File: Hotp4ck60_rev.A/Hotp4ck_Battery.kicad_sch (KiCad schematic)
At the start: 16 parts, among them J3 Conn_01x02_MountingPin, Q1 AO3401A, SW2 PWR, U3 MAX17048, U3 TP4056

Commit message: Fixed path
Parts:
- renumbered C21 to C22, C23 to C24
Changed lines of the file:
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@@
   (symbol (lib_id "Device:C_Small") (at 40.64 53.34 0) (unit 1)
     (in_bom yes) (on_board yes) (dnp no)
-    (property "Reference" "C21" (at 40.64 45.72 0)
+    (property "Reference" "C22" (at 40.64 45.72 0)
       (effects (font (size 1.27 1.27)))
     )
@@
       (project "Hotp4ck60"
         (path "/a57939d7-40ce-4436-8014-db245ef7f3c5/18c06ada-111b-4ec0-9dc0-78c3052676b0"
-          (reference "C21") (unit 1)
+          (reference "C22") (unit 1)
         )
       )
@@
   (symbol (lib_id "Device:C_Small") (at 83.82 119.38 0) (unit 1)
     (in_bom yes) (on_board yes) (dnp no) (fields_autoplaced)
-    (property "Reference" "C27" (at 81.28 118.1162 0)
-      (effects (font (size 1.27 1.27)) (justify right))
-    )
-    (property "Value" "100 nF" (at 81.28 120.6562 0)
-      (effects (font (size 1.27 1.27)) (justify right))
+    (property "Reference" "C27" (at 86.36 118.1163 0)
+      (effects (font (size 1.27 1.27)) (justify left))
+    )
+    (property "Value" "100 nF" (at 86.36 120.6563 0)
+      (effects (font (size 1.27 1.27)) (justify left))
     )
     (property "Footprint" "Capacitor_SMD:C_0402_1005Metric" (at 83.82 119.38 0)
@@
         )
         (path "/a57939d7-40ce-4436-8014-db245ef7f3c5/18c06ada-111b-4ec0-9dc0-78c3052676b0"
-          (reference "C27") (unit 1)
+          (reference "C25") (unit 1)
         )
       )
@@
   (symbol (lib_id "Device:C_Small") (at 77.47 53.34 0) (unit 1)
     (in_bom yes) (on_board yes) (dnp no)
-    (property "Reference" "C23" (at 73.66 52.07 0)
+    (property "Reference" "C24" (at 73.66 52.07 0)
       (effects (font (size 1.27 1.27)) (justify right))
     )
@@
       (project "Hotp4ck60"
         (path "/a57939d7-40ce-4436-8014-db245ef7f3c5/18c06ada-111b-4ec0-9dc0-78c3052676b0"
+          (reference "C24") (unit 1)
+        )
+      )
+      (project "designguide-schematic"
+        (path "/c2a65ddb-3915-4293-98a9-444287fe2a3d"
+          (reference "C2") (unit 1)
+        )
+      )
+    )
+  )
+  (symbol (lib_id "Device:R_Small") (at 35.56 58.42 0) (unit 1)
+    (in_bom yes) (on_board yes) (dnp no)
+    (property "Reference" "R6" (at 29.21 57.15 0)
+      (effects (font (size 1.27 1.27)) (justify left))
+    )
+    (property "Value" "1.5 kOhm" (at 25.4 59.69 0)
+      (effects (font (size 1.27 1.27)) (justify left))
+    )
+    (property "Footprint" "Resistor_SMD:R_0402_1005Metric" (at 35.56 58.42 0)
+      (effects (font (size 1.27 1.27)) hide)
+    )
+    (property "Datasheet" "~" (at 35.56 58.42 0)
+      (effects (font (size 1.27 1.27)) hide)
+    )
+    (property "LCSC" "C25792" (at 35.56 58.42 0)
+      (effects (font (size 1.27 1.27)) hide)
+    )
+    (pin "1")
+    (pin "2")
+    (instances
+      (project "osprey_rev_a"
+        (path "/86a516b3-939b-48ee-9a25-d0111c577d06/e12a0b82-f794-4b5e-b657-628292a2530a"
+          (reference "R6") (unit 1)
+        )
+      )
+      (project "Hotp4ck60"
+        (path "/a57939d7-40ce-4436-8014-db245ef7f3c5"
+          (reference "R3") (unit 1)
+        )
+        (path "/a57939d7-40ce-4436-8014-db245ef7f3c5/18c06ada-111b-4ec0-9dc0-78c3052676b0"
+          (reference "R3") (unit 1)
+        )
+      )
+      (project "designguide-schematic"
+        (path "/c2a65ddb-3915-4293-98a9-444287fe2a3d"
+          (reference "R5") (unit 1)
+        )
+      )
+    )
+  )
+  (symbol (lib_id "Device:C_Small") (at 46.99 53.34 0) (unit 1)
+    (in_bom yes) (on_board yes) (dnp no)
+    (property "Reference" "C22" (at 46.99 45.72 0)
+      (effects (font (size 1.27 1.27)))
+    )
+    (property "Value" "4.7 uF" (at 46.99 48.26 0)
+      (effects (font (size 1.27 1.27)))
+    )
+    (property "Footprint" "Capacitor_SMD:C_0402_1005Metric" (at 46.99 53.34 0)
+      (effects (font (size 1.27 1.27)) hide)
+    )
+    (property "Datasheet" "~" (at 46.99 53.34 0)
+      (effects (font (size 1.27 1.27)) hide)
+    )
+    (property "LCSC" "C52923" (at 46.99 53.34 0)
+      (effects (font (size 1.27 1.27)) hide)
+    )
+    (property "Notes" "X7R, 10%" (at 46.99 53.34 0)
+      (effects (font (size 1.27 1.27)) hide)
+    )
+    (pin "1")
+    (pin "2")
+    (instances
+      (project "osprey_rev_a"
+        (path "/86a516b3-939b-48ee-9a25-d0111c577d06/e12a0b82-f794-4b5e-b657-628292a2530a"
+          (reference "C22") (unit 1)
+        )
+      )
+      (project "Hotp4ck60"
+        (path "/a57939d7-40ce-4436-8014-db245ef7f3c5"
+          (reference "C22") (unit 1)
+        )
+        (path "/a57939d7-40ce-4436-8014-db245ef7f3c5/18c06ada-111b-4ec0-9dc0-78c3052676b0"
           (reference "C23") (unit 1)
         )
       )
-      (project "designguide-schematic"
-        (path "/c2a65ddb-3915-4293-98a9-444287fe2a3d"
-          (reference "C2") (unit 1)
-        )
-      )
-    )
-  )
-  (symbol (lib_id "Device:R_Small") (at 35.56 58.42 0) (unit 1)
-    (in_bom yes) (on_board yes) (dnp no)
-    (property "Reference" "R6" (at 29.21 57.15 0)
-      (effects (font (size 1.27 1.27)) (justify left))
-    )
-    (property "Value" "1.5 kOhm" (at 25.4 59.69 0)
-      (effects (font (size 1.27 1.27)) (justify left))
-    )
-    (property "Footprint" "Resistor_SMD:R_0402_1005Metric" (at 35.56 58.42 0)
-      (effects (font (size 1.27 1.27)) hide)
-    )
-    (property "Datasheet" "~" (at 35.56 58.42 0)
-      (effects (font (size 1.27 1.27)) hide)
-    )
-    (property "LCSC" "C25792" (at 35.56 58.42 0)
-      (effects (font (size 1.27 1.27)) hide)
-    )
-    (pin "1")
-    (pin "2")
-    (instances
-      (project "osprey_rev_a"
-        (path "/86a516b3-939b-48ee-9a25-d0111c577d06/e12a0b82-f794-4b5e-b657-628292a2530a"
-          (reference "R6") (unit 1)
-        )
-      )
-      (project "Hotp4ck60"
-        (path "/a57939d7-40ce-4436-8014-db245ef7f3c5"
-          (reference "R3") (unit 1)
-        )
-        (path "/a57939d7-40ce-4436-8014-db245ef7f3c5/18c06ada-111b-4ec0-9dc0-78c3052676b0"
-          (reference "R3") (unit 1)
-        )
-      )
-      (project "designguide-schematic"
-        (path "/c2a65ddb-3915-4293-98a9-444287fe2a3d"
-          (reference "R5") (unit 1)
-        )
-      )
-    )
-  )
-  (symbol (lib_id "Device:C_Small") (at 46.99 53.34 0) (unit 1)
-    (in_bom yes) (on_board yes) (dnp no)
-    (property "Reference" "C22" (at 46.99 45.72 0)
-      (effects (font (size 1.27 1.27)))
-    )
-    (property "Value" "4.7 uF" (at 46.99 48.26 0)
-      (effects (font (size 1.27 1.27)))
-    )
-    (property "Footprint" "Capacitor_SMD:C_0402_1005Metric" (at 46.99 53.34 0)
-      (effects (font (size 1.27 1.27)) hide)
-    )
-    (property "Datasheet" "~" (at 46.99 53.34 0)
-      (effects (font (size 1.27 1.27)) hide)
-    )
-    (property "LCSC" "C52923" (at 46.99 53.34 0)
-      (effects (font (size 1.27 1.27)) hide)
-    )
-    (property "Notes" "X7R, 10%" (at 46.99 53.34 0)
-      (effects (font (size 1.27 1.27)) hide)
-    )
-    (pin "1")
-    (pin "2")
-    (instances
-      (project "osprey_rev_a"
-        (path "/86a516b3-939b-48ee-9a25-d0111c577d06/e12a0b82-f794-4b5e-b657-628292a2530a"
-          (reference "C22") (unit 1)
-        )
-      )
-      (project "Hotp4ck60"
-        (path "/a57939d7-40ce-4436-8014-db245ef7f3c5"
-          (reference "C22") (unit 1)
-        )
-        (path "/a57939d7-40ce-4436-8014-db245ef7f3c5/18c06ada-111b-4ec0-9dc0-78c3052676b0"
-          (reference "C22") (unit 1)
-        )
-      )

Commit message: Modified positions
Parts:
- renumbered C22 to C21, C24 to C23
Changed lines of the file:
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@@
   (symbol (lib_id "Device:C_Small") (at 40.64 53.34 0) (unit 1)
     (in_bom yes) (on_board yes) (dnp no)
-    (property "Reference" "C22" (at 40.64 45.72 0)
+    (property "Reference" "C21" (at 40.64 45.72 0)
       (effects (font (size 1.27 1.27)))
     )
@@
       (project "Hotp4ck60"
         (path "/a57939d7-40ce-4436-8014-db245ef7f3c5/18c06ada-111b-4ec0-9dc0-78c3052676b0"
-          (reference "C22") (unit 1)
+          (reference "C21") (unit 1)
         )
       )
@@
         )
         (path "/a57939d7-40ce-4436-8014-db245ef7f3c5/18c06ada-111b-4ec0-9dc0-78c3052676b0"
-          (reference "C25") (unit 1)
+          (reference "C24") (unit 1)
         )
       )
@@
   (symbol (lib_id "Device:C_Small") (at 77.47 53.34 0) (unit 1)
     (in_bom yes) (on_board yes) (dnp no)
-    (property "Reference" "C24" (at 73.66 52.07 0)
+    (property "Reference" "C23" (at 73.66 52.07 0)
       (effects (font (size 1.27 1.27)) (justify right))
     )
@@
       (project "Hotp4ck60"
         (path "/a57939d7-40ce-4436-8014-db245ef7f3c5/18c06ada-111b-4ec0-9dc0-78c3052676b0"
-          (reference "C24") (unit 1)
+          (reference "C23") (unit 1)
         )
       )
@@
         )
         (path "/a57939d7-40ce-4436-8014-db245ef7f3c5/18c06ada-111b-4ec0-9dc0-78c3052676b0"
-          (reference "C23") (unit 1)
-        )
-      )
+          (reference "C22") (unit 1)
+        )
+      )

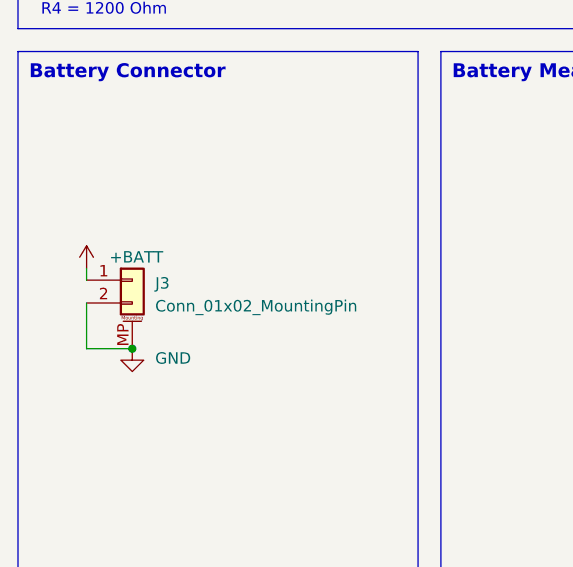
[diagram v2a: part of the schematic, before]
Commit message: unified daughterboard, MCU 추가
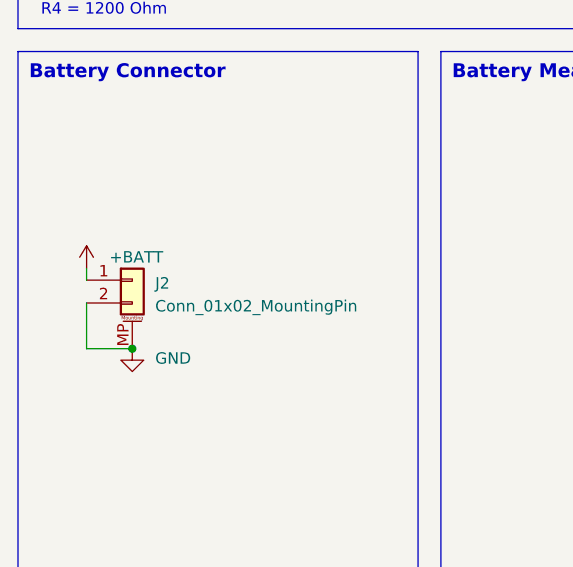
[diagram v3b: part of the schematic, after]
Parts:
- renumbered J3 to J2

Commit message: 리비젼A 수정
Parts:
- removed J2: Conn_01x02_MountingPin, Connector_Molex:Molex_PicoBlade_53261-0271_1x02-1MP_P1.25mm_Horizontal, symbol Connector_Generic_MountingPin:Conn_01x02_MountingPin
- removed SW2: PWR, marbastlib-various:SW_MSK12C02-HB, symbol Connector_Generic_MountingPin:Conn_01x03_MountingPin
- added SW2: SW_DIP_x01, Hotp4ck:SW_DIP_HOTP4CK, symbol Switch:SW_DIP_x01
- renumbered C27 to C24, R6 to R3, R7 to R4, R7 to R6, R1 to R7, R2 to R8, U3 to U4
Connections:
- net +BATT: now also SW2.1
- net at Q1.3 (D): now also SW2.2
- no-connect marks 2 -> 1

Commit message: 배선 완료
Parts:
- removed LED2: Yellow, LED_SMD:LED_0603_1608Metric, symbol Device:LED_Small
- removed U3: TP4056, Package_SO:SOIC-8-1EP_3.9x4.9mm_P1.27mm_EP2.29x3mm, symbol marbastlib-various:TP4056
- added C24, C26: 4u7, Capacitor_SMD:C_0402_1005Metric, symbol Device:C_Small
- added C25, C27: 1u, Capacitor_SMD:C_0402_1005Metric, symbol Device:C_Small
- added R1: 68k, Resistor_SMD:R_0805_2012Metric, symbol Device:R_Small
- added R2: 1k5, Resistor_SMD:R_0402_1005Metric, symbol Device:R_Small
- added U2: BQ24075RGT, Package_DFN_QFN:VQFN-16-1EP_3x3mm_P0.5mm_EP1.6x1.6mm, symbol Battery_Management:BQ24075RGT
- C21, C23: value 10 uF -> 4u7; footprint Capacitor_SMD:C_0805_2012Metric -> Capacitor_SMD:C_0402_1005Metric; LCSC (none) -> C23733
- C22: value 4.7 uF -> 4u7; LCSC C52923 -> C23733; Notes X7R, 10% -> (none)
- R3: value 1.5 kOhm -> 2k2; LCSC C25792 -> C25879
- R4: value 1.2 kOhm -> 10k; LCSC C25867 -> C25744
- U4: now left out of the parts list
- renumbered C24 to C7, R6 to R5, R7 to R6, R8 to R7
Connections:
- net +5V: now also C23.1, U2.13 (IN)
- net +BATT: now also C26.1, C27.1, U2.2 (BAT), U2.3 (BAT); no longer C23.1
- net +VSW: now also C24.1, C25.1, U2.10 (OUT), U2.11 (OUT), U2.6 (EN1)
- net GND: now also R3.2, C24.2, C25.2, C26.2, C27.2, R1.2, R2.2, U2.15 (SYSOFF), U2.17 (VSS), U2.4 (~{CE}), U2.5 (EN2), U2.8 (VSS)
- net at R4.1: now also U2.1 (TS)
- net at R3.1: now also U2.16 (ISET)
- new net: R2.1, U2.12 (ILIM)
- new net: R1.1, U2.14 (TMR)
- new net ~{CHG}: U2.9 (~{CHG})
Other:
- note removed: "1 A = 1 V / R4 * 1200 R4 = 1200 Ohm"
- note removed: "BAT"
- note removed: "I = V / R * 1200"
- note removed: "PROG"
- moved on the sheet: C7, D65, Q1, R5, R6, R7, SW2, U4
